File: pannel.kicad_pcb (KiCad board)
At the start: 2 copper layers, 98.5 x 80 mm, 254 parts, among them J1 USB_B_Micro, J2 AVR-ISP-6, J3 Conn_01x03_Male, SW1 SW_SPDT, SW2 SW_SPDT, U1 ATmega32U4-AU, U2 TLV1117-33, Y1 16MHz

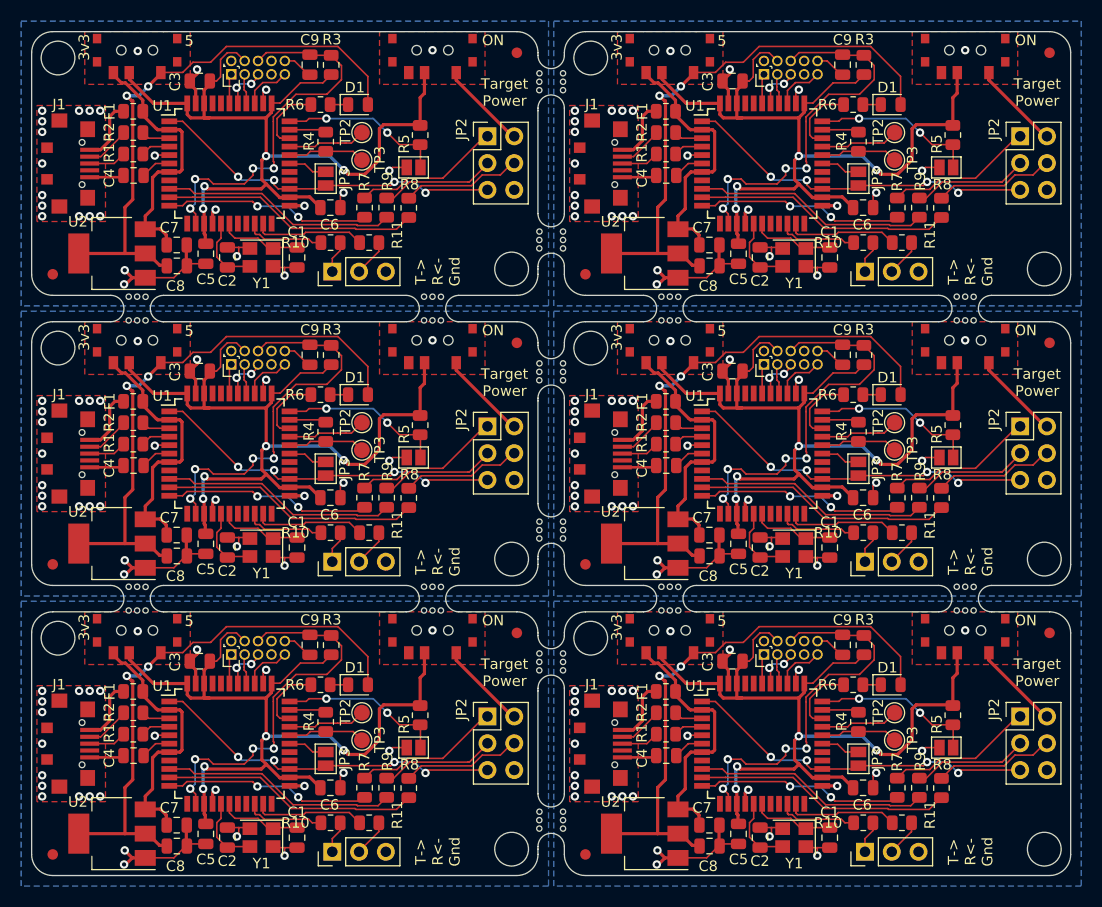
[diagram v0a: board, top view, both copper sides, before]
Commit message: Fixed ground fill on pannel
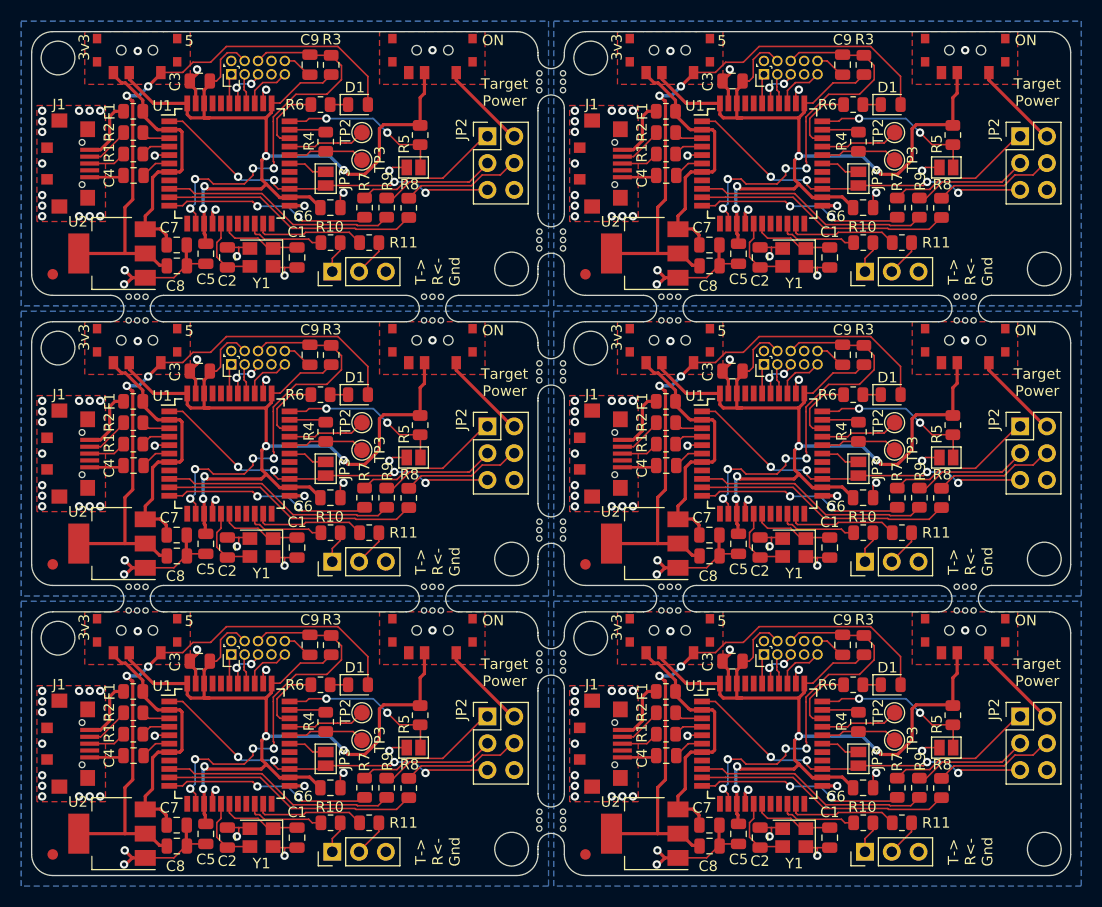
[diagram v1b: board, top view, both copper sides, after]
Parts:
- removed FID2 (x6): Fiducial, Fiducial:Fiducial_1mm_Mask2mm

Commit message: at some point i will be good at boards
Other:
- board text added: "Rev 1.0, Sep 2021 github.com/timChase98/ WetAvrProgrammer"
- board text removed: "Rev 1.0, Sep 2021 github.com/timChase98/WetAvrProgrammer"
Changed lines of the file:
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@@
     (effects (font (size 1 1) (thickness 0.15)))
   )
-  (gr_text "Rev 1.0,  Sep 2021\ngithub.com/timChase98/WetAvrProgrammer\n" (at 54.1068 -2.6924) (layer B.SilkS)
-    (effects (font (size 1 1) (thickness 0.1524)) (justify right mirror))
+  (gr_text "Rev 1.0,  Sep 2021\ngithub.com/timChase98/\nWetAvrProgrammer\n" (at 91.5 -6.75) (layer B.SilkS)
+    (effects (font (size 1 1) (thickness 0.1524)) (justify left mirror))
   )
   (gr_text "Target\nPower\n" (at 95.331 -19.2405) (layer F.SilkS)
@@
     (effects (font (size 1 1) (thickness 0.15)))
   )
-  (gr_text "Rev 1.0,  Sep 2021\ngithub.com/timChase98/WetAvrProgrammer\n" (at 54.1068 -30.1924) (layer B.SilkS)
-    (effects (font (size 1 1) (thickness 0.1524)) (justify right mirror))
+  (gr_text "Rev 1.0,  Sep 2021\ngithub.com/timChase98/\nWetAvrProgrammer\n" (at 91.5 -34.25) (layer B.SilkS)
+    (effects (font (size 1 1) (thickness 0.1524)) (justify left mirror))
   )
   (gr_text "Target\nPower\n" (at 95.331 -46.7405) (layer F.SilkS)
@@
     (effects (font (size 1 1) (thickness 0.15)))
   )
-  (gr_text "Rev 1.0,  Sep 2021\ngithub.com/timChase98/WetAvrProgrammer\n" (at 54.1068 -57.6924) (layer B.SilkS)
-    (effects (font (size 1 1) (thickness 0.1524)) (justify right mirror))
+  (gr_text "Rev 1.0,  Sep 2021\ngithub.com/timChase98/\nWetAvrProgrammer\n" (at 91.5 -61.75) (layer B.SilkS)
+    (effects (font (size 1 1) (thickness 0.1524)) (justify left mirror))
   )
   (gr_text "Target\nPower\n" (at 95.331 -74.2405) (layer F.SilkS)
@@
     (effects (font (size 1 1) (thickness 0.15)))
   )
-  (gr_text "Rev 1.0,  Sep 2021\ngithub.com/timChase98/WetAvrProgrammer\n" (at 3.6068 -57.6924) (layer B.SilkS)
-    (effects (font (size 1 1) (thickness 0.1524)) (justify right mirror))
+  (gr_text "Rev 1.0,  Sep 2021\ngithub.com/timChase98/\nWetAvrProgrammer\n" (at 41 -61.75) (layer B.SilkS)
+    (effects (font (size 1 1) (thickness 0.1524)) (justify left mirror))
   )
   (gr_text "Target\nPower\n" (at 44.831 -74.2405) (layer F.SilkS)
@@
     (effects (font (size 1 1) (thickness 0.15)))
   )
-  (gr_text "Rev 1.0,  Sep 2021\ngithub.com/timChase98/WetAvrProgrammer\n" (at 3.6068 -30.1924) (layer B.SilkS)
-    (effects (font (size 1 1) (thickness 0.1524)) (justify right mirror))
+  (gr_text "Rev 1.0,  Sep 2021\ngithub.com/timChase98/\nWetAvrProgrammer\n" (at 41 -34.25) (layer B.SilkS)
+    (effects (font (size 1 1) (thickness 0.1524)) (justify left mirror))
   )
   (gr_text "Target\nPower\n" (at 44.831 -46.7405) (layer F.SilkS)
@@
     (effects (font (size 1 1) (thickness 0.15)))
   )
-  (gr_text "Rev 1.0,  Sep 2021\ngithub.com/timChase98/WetAvrProgrammer\n" (at 3.6068 -2.6924) (layer B.SilkS)
-    (effects (font (size 1 1) (thickness 0.1524)) (justify right mirror))
+  (gr_text "Rev 1.0,  Sep 2021\ngithub.com/timChase98/\nWetAvrProgrammer\n" (at 41 -6.75) (layer B.SilkS)
+    (effects (font (size 1 1) (thickness 0.1524)) (justify left mirror))
   )
   (gr_text "Target\nPower\n" (at 44.831 -19.2405) (layer F.SilkS)

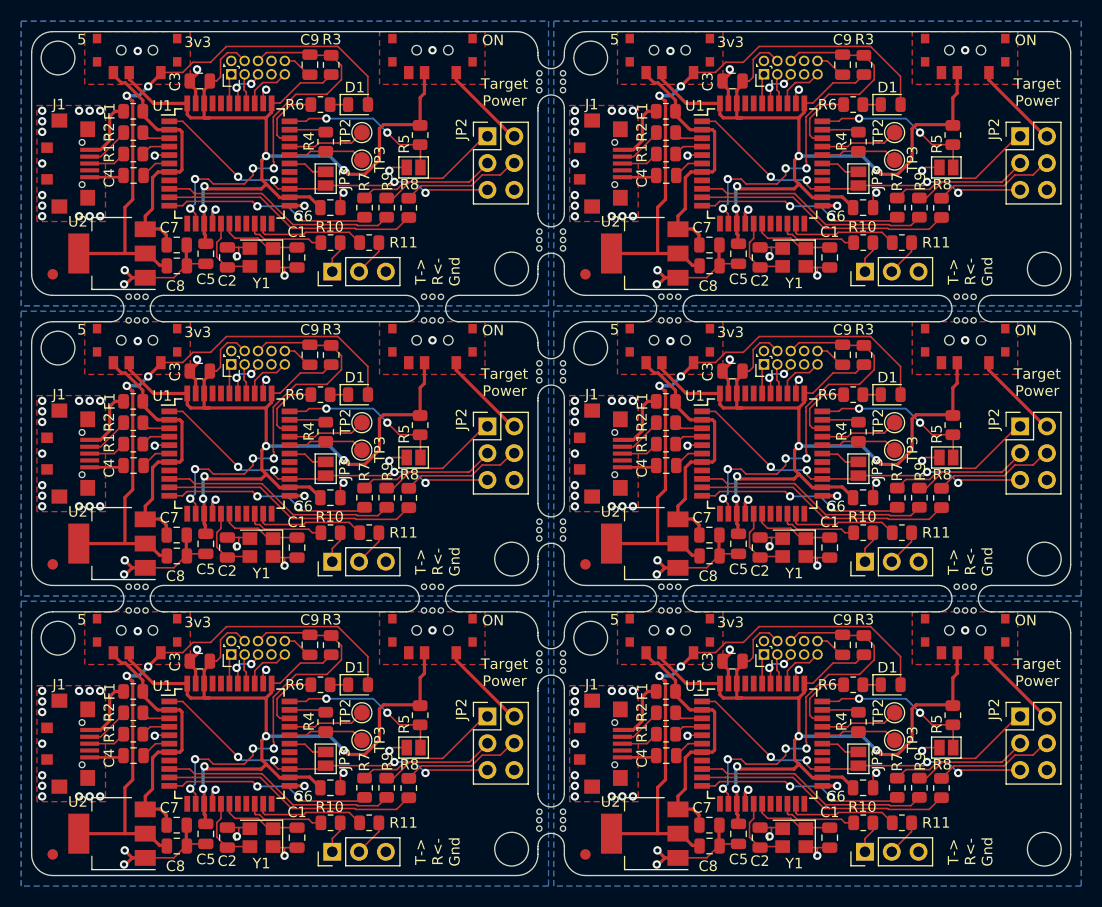
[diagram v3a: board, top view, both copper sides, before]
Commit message: Fixed Switch Labels
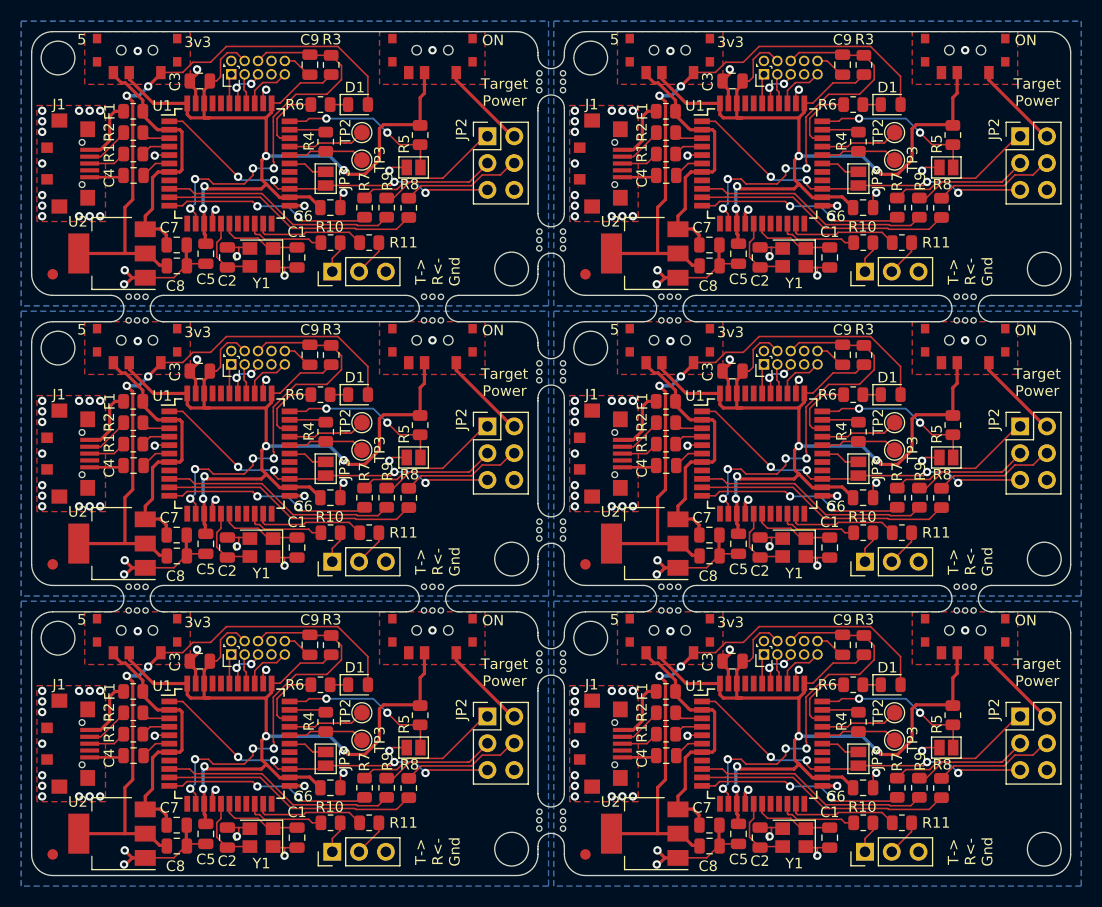
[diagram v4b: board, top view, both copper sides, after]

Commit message: Fixed Switch Labels
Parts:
- added FID2: Fiducial, Fiducial:Fiducial_1mm_Mask2mm, F.Cu at (96.5, -78.0)
- added FID2: Fiducial, Fiducial:Fiducial_1mm_Mask2mm, F.Cu at (96.5, -50.5)
- added FID2: Fiducial, Fiducial:Fiducial_1mm_Mask2mm, F.Cu at (96.5, -23.0)
- added FID2: Fiducial, Fiducial:Fiducial_1mm_Mask2mm, F.Cu at (46.0, -23.0)
- added FID2: Fiducial, Fiducial:Fiducial_1mm_Mask2mm, F.Cu at (46.0, -50.5)
- added FID2: Fiducial, Fiducial:Fiducial_1mm_Mask2mm, F.Cu at (46.0, -78.0)
